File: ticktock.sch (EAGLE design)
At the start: 53 parts, among them IC1 ATMEGA644A, IC2 AD8611R, IC3 REF200U, J1 AVR_SPI_PRG_6NS, Q1 MOSFET-NCHANNEL2N7002PW, Q2 MOSFET-NCHANNELBSS138, Q3 MOSFET-NCHANNELBSS138, U1 MAX232SOIC16, U2 OSCILLATORSMD, U3 FT232RLSSOP, U4 BMP180

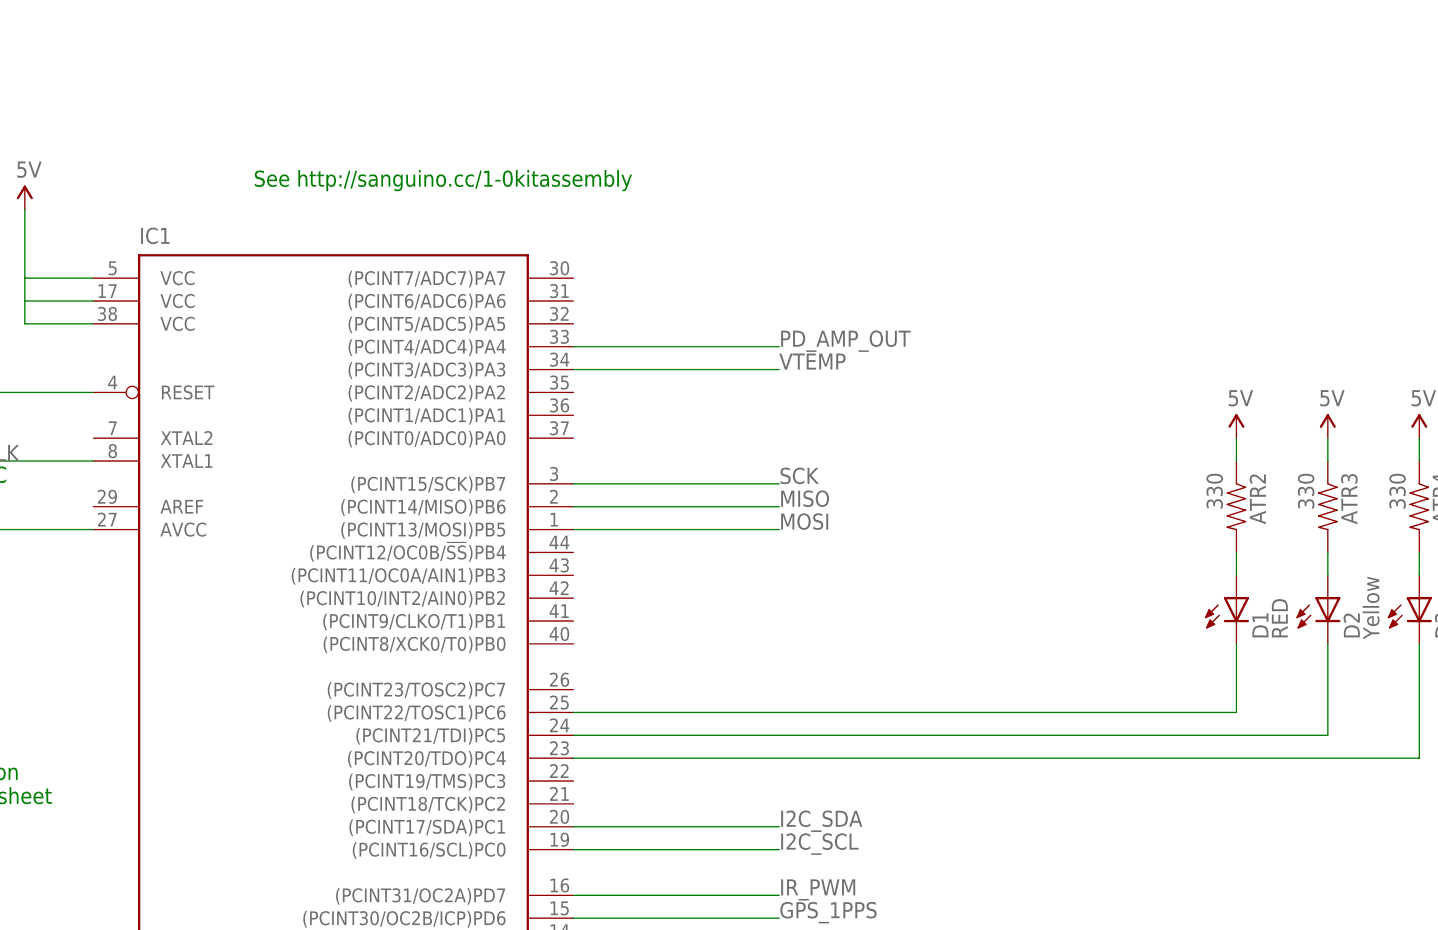
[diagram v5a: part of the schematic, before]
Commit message: Add test points
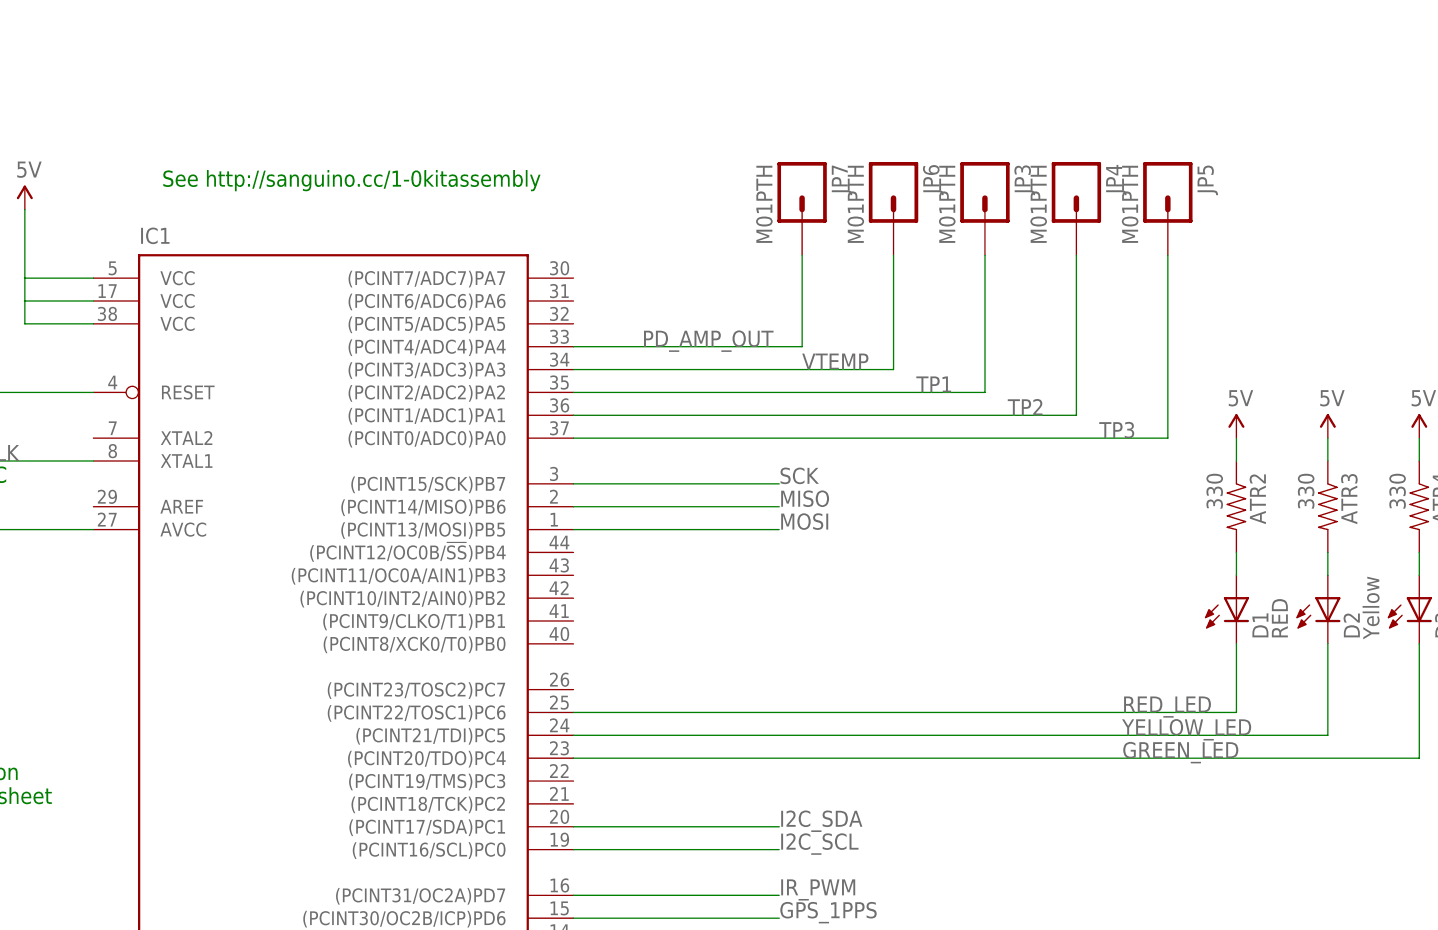
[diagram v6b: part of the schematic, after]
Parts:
- added JP3, JP4, JP5, JP6, JP7: M01PTH, SparkFun-Connectors:M01PTH
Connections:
- net N$23 renamed YELLOW_LED
- net N$24 renamed GREEN_LED
- net N$25 renamed RED_LED
- new net TP1: IC1.(PCINT2/ADC2)PA2, JP3.1
- new net TP2: IC1.(PCINT1/ADC1)PA1, JP4.1
- new net TP3: IC1.(PCINT0/ADC0)PA0, JP5.1
- net PD_AMP_OUT: now also JP7.1
- net VTEMP: now also JP6.1
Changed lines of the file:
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@@
 <part name="SUPPLY29" library="SparkFun-Aesthetics" deviceset="5V" device=""/>
 <part name="SUPPLY30" library="SparkFun-Aesthetics" deviceset="5V" device=""/>
+<part name="JP3" library="SparkFun-Connectors" deviceset="M01" device="PTH"/>
+<part name="JP4" library="SparkFun-Connectors" deviceset="M01" device="PTH"/>
+<part name="JP5" library="SparkFun-Connectors" deviceset="M01" device="PTH"/>
+<part name="JP6" library="SparkFun-Connectors" deviceset="M01" device="PTH"/>
+<part name="JP7" library="SparkFun-Connectors" deviceset="M01" device="PTH"/>
 </parts>
 <sheets>
@@
 <text x="88.9" y="162.56" size="1.778" layer="91">XTAL2 is NC
 See Fig 9-4</text>
-<text x="129.54" y="198.12" size="1.778" layer="91">See http://sanguino.cc/1-0kitassembly</text>
+<text x="119.38" y="198.12" size="1.778" layer="91">See http://sanguino.cc/1-0kitassembly</text>
 <text x="238.76" y="99.06" size="1.778" layer="91">Jumper 1-2 for GPS
 Jumper 2-3 for LOCAL</text>
@@
 <instance part="SUPPLY29" gate="G$1" x="248.92" y="170.18"/>
 <instance part="SUPPLY30" gate="G$1" x="259.08" y="170.18"/>
+<instance part="JP3" gate="G$1" x="210.82" y="198.12" rot="R270"/>
+<instance part="JP4" gate="G$1" x="220.98" y="198.12" rot="R270"/>
+<instance part="JP5" gate="G$1" x="231.14" y="198.12" rot="R270"/>
+<instance part="JP6" gate="G$1" x="200.66" y="198.12" rot="R270"/>
+<instance part="JP7" gate="G$1" x="190.5" y="198.12" rot="R270"/>
 </instances>
 <busses>
@@
 <segment>
 <pinref part="IC1" gate="G$1" pin="(PCINT4/ADC4)PA4"/>
-<wire x1="165.1" y1="180.34" x2="187.96" y2="180.34" width="0.1524" layer="91"/>
-<label x="187.96" y="180.34" size="1.778" layer="95"/>
+<wire x1="165.1" y1="180.34" x2="190.5" y2="180.34" width="0.1524" layer="91"/>
+<label x="172.72" y="180.34" size="1.778" layer="95"/>
+<pinref part="JP7" gate="G$1" pin="1"/>
+<wire x1="190.5" y1="180.34" x2="190.5" y2="190.5" width="0.1524" layer="91"/>
 </segment>
 </net>
@@
 <segment>
 <pinref part="IC1" gate="G$1" pin="(PCINT3/ADC3)PA3"/>
-<wire x1="165.1" y1="177.8" x2="187.96" y2="177.8" width="0.1524" layer="91"/>
-<label x="187.96" y="177.8" size="1.778" layer="95"/>
+<wire x1="165.1" y1="177.8" x2="200.66" y2="177.8" width="0.1524" layer="91"/>
+<label x="190.5" y="177.8" size="1.778" layer="95"/>
+<pinref part="JP6" gate="G$1" pin="1"/>
+<wire x1="200.66" y1="190.5" x2="200.66" y2="177.8" width="0.1524" layer="91"/>
 </segment>
 </net>
@@
 </segment>
 </net>
-<net name="N$23" class="0">
+<net name="YELLOW_LED" class="0">
 <segment>
 <pinref part="D2" gate="G$1" pin="C"/>
@@
 <pinref part="IC1" gate="G$1" pin="(PCINT21/TDI)PC5"/>
 <wire x1="248.92" y1="137.16" x2="165.1" y2="137.16" width="0.1524" layer="91"/>
-</segment>
-</net>
-<net name="N$24" class="0">
+<label x="226.06" y="137.16" size="1.778" layer="95"/>
+</segment>
+</net>
+<net name="GREEN_LED" class="0">
 <segment>
 <pinref part="D3" gate="G$1" pin="C"/>
@@
 <pinref part="IC1" gate="G$1" pin="(PCINT20/TDO)PC4"/>
 <wire x1="165.1" y1="134.62" x2="259.08" y2="134.62" width="0.1524" layer="91"/>
-</segment>
-</net>
-<net name="N$25" class="0">
+<label x="226.06" y="134.62" size="1.778" layer="95"/>
+</segment>
+</net>
+<net name="RED_LED" class="0">
 <segment>
 <pinref part="IC1" gate="G$1" pin="(PCINT22/TOSC1)PC6"/>
 <wire x1="165.1" y1="139.7" x2="238.76" y2="139.7" width="0.1524" layer="91"/>
-</segment>
-</net>
+<label x="226.06" y="139.7" size="1.778" layer="95"/>
+</segment>
+</net>
+<net name="TP1" class="0">
+<segment>
+<pinref part="JP3" gate="G$1" pin="1"/>
+<wire x1="210.82" y1="190.5" x2="210.82" y2="175.26" width="0.1524" layer="91"/>
+<pinref part="IC1" gate="G$1" pin="(PCINT2/ADC2)PA2"/>
+<wire x1="210.82" y1="175.26" x2="165.1" y2="175.26" width="0.1524" layer="91"/>
+<label x="203.2" y="175.26" size="1.778" layer="95"/>
+</segment>
+</net>
+<net name="TP2" class="0">
+<segment>
+<pinref part="IC1" gate="G$1" pin="(PCINT1/ADC1)PA1"/>
+<wire x1="165.1" y1="172.72" x2="220.98" y2="172.72" width="0.1524" layer="91"/>
+<pinref part="JP4" gate="G$1" pin="1"/>
+<wire x1="220.98" y1="172.72" x2="220.98" y2="190.5" width="0.1524" layer="91"/>
+<label x="213.36" y="172.72" size="1.778" layer="95"/>
+</segment>
+</net>
+<net name="TP3" class="0">
+<segment>
+<pinref part="JP5" gate="G$1" pin="1"/>
+<wire x1="231.14" y1="190.5" x2="231.14" y2="170.18" width="0.1524" layer="91"/>
+<pinref part="IC1" gate="G$1" pin="(PCINT0/ADC0)PA0"/>
+<wire x1="231.14" y1="170.18" x2="165.1" y2="170.18" width="0.1524" layer="91"/>
+<label x="223.52" y="170.18" size="1.778" layer="95"/>
+</segment>
+</net>

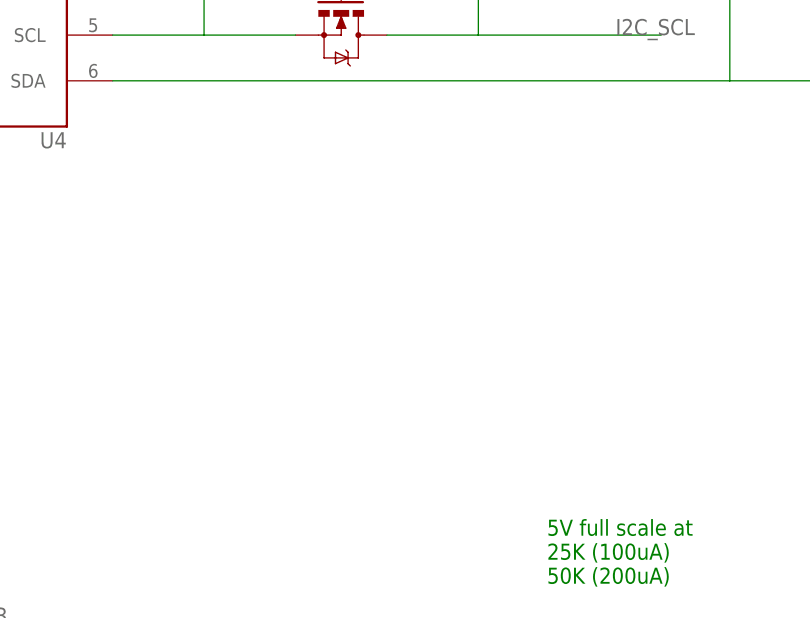
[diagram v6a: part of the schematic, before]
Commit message: Add header for fallback BMP085 carrier board
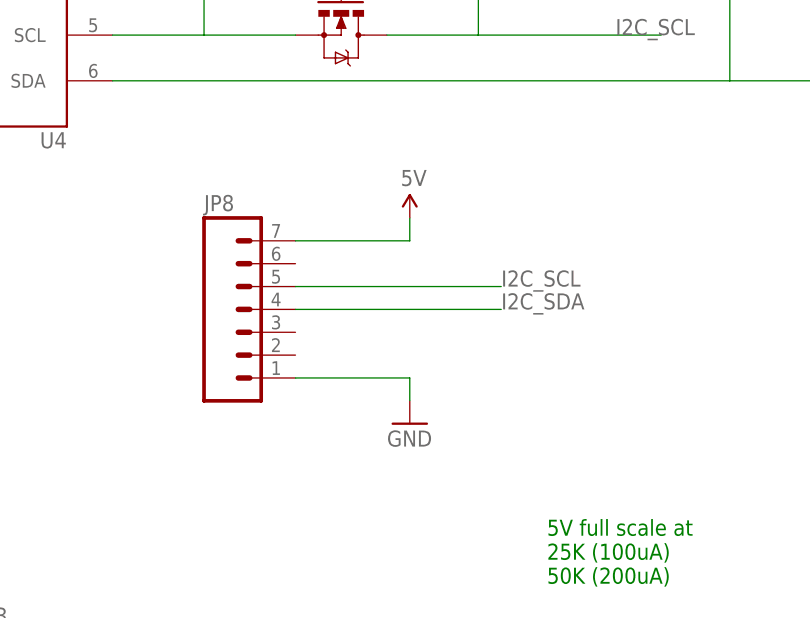
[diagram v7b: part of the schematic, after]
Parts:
- added JP8: (no value), SparkFun-Connectors:M07LOCK
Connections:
- net 5V: now also JP8.7
- net GND: now also JP8.1
- net I2C_SCL: now also JP8.5
- net I2C_SDA: now also JP8.4
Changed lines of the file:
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@@
 <part name="JP6" library="SparkFun-Connectors" deviceset="M01" device="PTH"/>
 <part name="JP7" library="SparkFun-Connectors" deviceset="M01" device="PTH"/>
+<part name="JP8" library="SparkFun-Connectors" deviceset="M07" device="LOCK"/>
+<part name="SUPPLY31" library="SparkFun-Aesthetics" deviceset="5V" device=""/>
+<part name="GND25" library="SparkFun-Aesthetics" deviceset="GND" device=""/>
 </parts>
 <sheets>
@@
 <instance part="JP6" gate="G$1" x="200.66" y="198.12" rot="R270"/>
 <instance part="JP7" gate="G$1" x="190.5" y="198.12" rot="R270"/>
+<instance part="JP8" gate="G$1" x="403.86" y="111.76"/>
+<instance part="SUPPLY31" gate="G$1" x="421.64" y="124.46"/>
+<instance part="GND25" gate="1" x="421.64" y="101.6"/>
 </instances>
 <busses>
@@
 <wire x1="353.06" y1="162.56" x2="355.6" y2="162.56" width="0.1524" layer="91"/>
 </segment>
+<segment>
+<pinref part="JP8" gate="G$1" pin="1"/>
+<wire x1="408.94" y1="106.68" x2="421.64" y2="106.68" width="0.1524" layer="91"/>
+<pinref part="GND25" gate="1" pin="GND"/>
+<wire x1="421.64" y1="106.68" x2="421.64" y2="104.14" width="0.1524" layer="91"/>
+</segment>
 </net>
 <net name="IR_PWM" class="0">
@@
 <pinref part="ATR4" gate="G$1" pin="1"/>
 <wire x1="259.08" y1="170.18" x2="259.08" y2="167.64" width="0.1524" layer="91"/>
+</segment>
+<segment>
+<pinref part="JP8" gate="G$1" pin="7"/>
+<wire x1="408.94" y1="121.92" x2="421.64" y2="121.92" width="0.1524" layer="91"/>
+<pinref part="SUPPLY31" gate="G$1" pin="5V"/>
+<wire x1="421.64" y1="121.92" x2="421.64" y2="124.46" width="0.1524" layer="91"/>
 </segment>
 </net>
@@
 <label x="187.96" y="124.46" size="1.778" layer="95"/>
 </segment>
+<segment>
+<pinref part="JP8" gate="G$1" pin="5"/>
+<wire x1="408.94" y1="116.84" x2="431.8" y2="116.84" width="0.1524" layer="91"/>
+<label x="431.8" y="116.84" size="1.778" layer="95"/>
+</segment>
 </net>
 <net name="N$18" class="0">
@@
 <label x="187.96" y="127" size="1.778" layer="95"/>
 </segment>
-</net>
+<segment>
+<pinref part="JP8" gate="G$1" pin="4"/>
+<wire x1="408.94" y1="114.3" x2="431.8" y2="114.3" width="0.1524" layer="91"/>
+<label x="431.8" y="114.3" size="1.778" layer="95"/>
+</segment>
+</net>

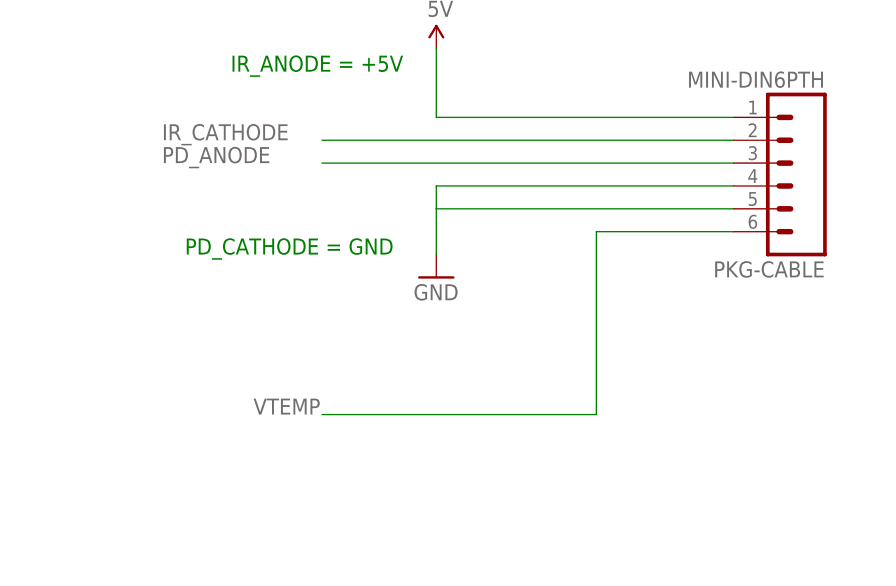
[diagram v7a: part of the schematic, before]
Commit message: Group sensors on mini-DIN
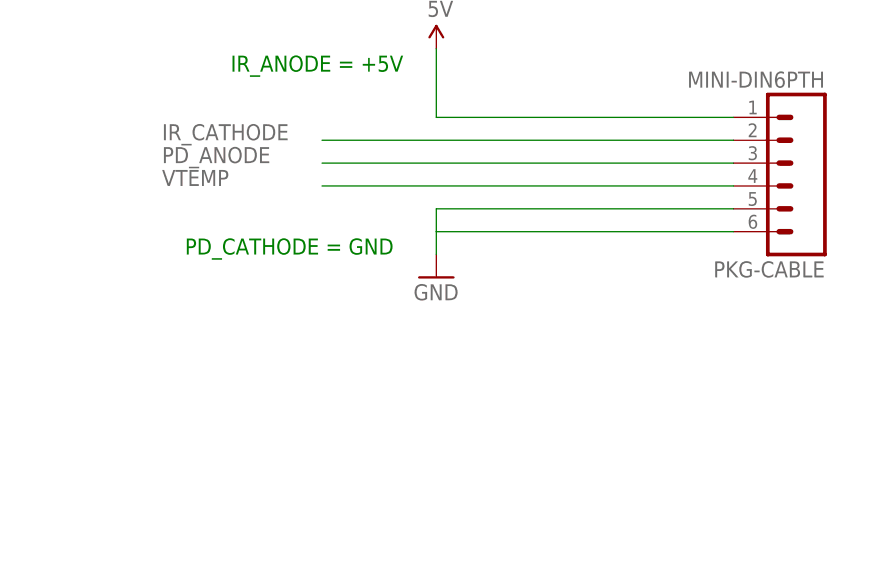
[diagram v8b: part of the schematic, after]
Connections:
- net GND: now also PKG-CABLE.6; no longer PKG-CABLE.4
- net VTEMP: now also PKG-CABLE.4; no longer PKG-CABLE.6
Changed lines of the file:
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@@
 </segment>
 <segment>
-<pinref part="PKG-CABLE" gate="G$1" pin="4"/>
-<wire x1="243.84" y1="406.4" x2="210.82" y2="406.4" width="0.1524" layer="91"/>
-<wire x1="210.82" y1="406.4" x2="210.82" y2="403.86" width="0.1524" layer="91"/>
 <pinref part="GND22" gate="1" pin="GND"/>
 <pinref part="PKG-CABLE" gate="G$1" pin="5"/>
-<wire x1="210.82" y1="403.86" x2="210.82" y2="398.78" width="0.1524" layer="91"/>
+<wire x1="210.82" y1="403.86" x2="210.82" y2="401.32" width="0.1524" layer="91"/>
+<wire x1="210.82" y1="401.32" x2="210.82" y2="398.78" width="0.1524" layer="91"/>
 <wire x1="243.84" y1="403.86" x2="210.82" y2="403.86" width="0.1524" layer="91"/>
+<pinref part="PKG-CABLE" gate="G$1" pin="6"/>
+<wire x1="243.84" y1="401.32" x2="210.82" y2="401.32" width="0.1524" layer="91"/>
 </segment>
 <segment>
@@
 <net name="VTEMP" class="0">
 <segment>
-<pinref part="PKG-CABLE" gate="G$1" pin="6"/>
-<wire x1="243.84" y1="401.32" x2="228.6" y2="401.32" width="0.1524" layer="91"/>
-<wire x1="228.6" y1="401.32" x2="228.6" y2="381" width="0.1524" layer="91"/>
-<wire x1="228.6" y1="381" x2="198.12" y2="381" width="0.1524" layer="91"/>
-<label x="190.5" y="381" size="1.778" layer="95"/>
-</segment>
-<segment>
 <pinref part="IC3" gate="G$1" pin="I1L"/>
 <wire x1="396.24" y1="71.12" x2="416.56" y2="71.12" width="0.1524" layer="91"/>
@@
 <wire x1="200.66" y1="190.5" x2="200.66" y2="177.8" width="0.1524" layer="91"/>
 </segment>
-</net>
+<segment>
+<pinref part="PKG-CABLE" gate="G$1" pin="4"/>
+<wire x1="243.84" y1="406.4" x2="198.12" y2="406.4" width="0.1524" layer="91"/>
+<label x="180.34" y="406.4" size="1.778" layer="95"/>
+</segment>
+</net>
